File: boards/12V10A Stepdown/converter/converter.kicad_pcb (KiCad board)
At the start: 2 copper layers, 27 parts, among them J1 TB005-762-02BE, J2 TB005-762-02BE, M1 CSD17578Q3A, M2 CSD17571Q2, U1 LM25145RGYR

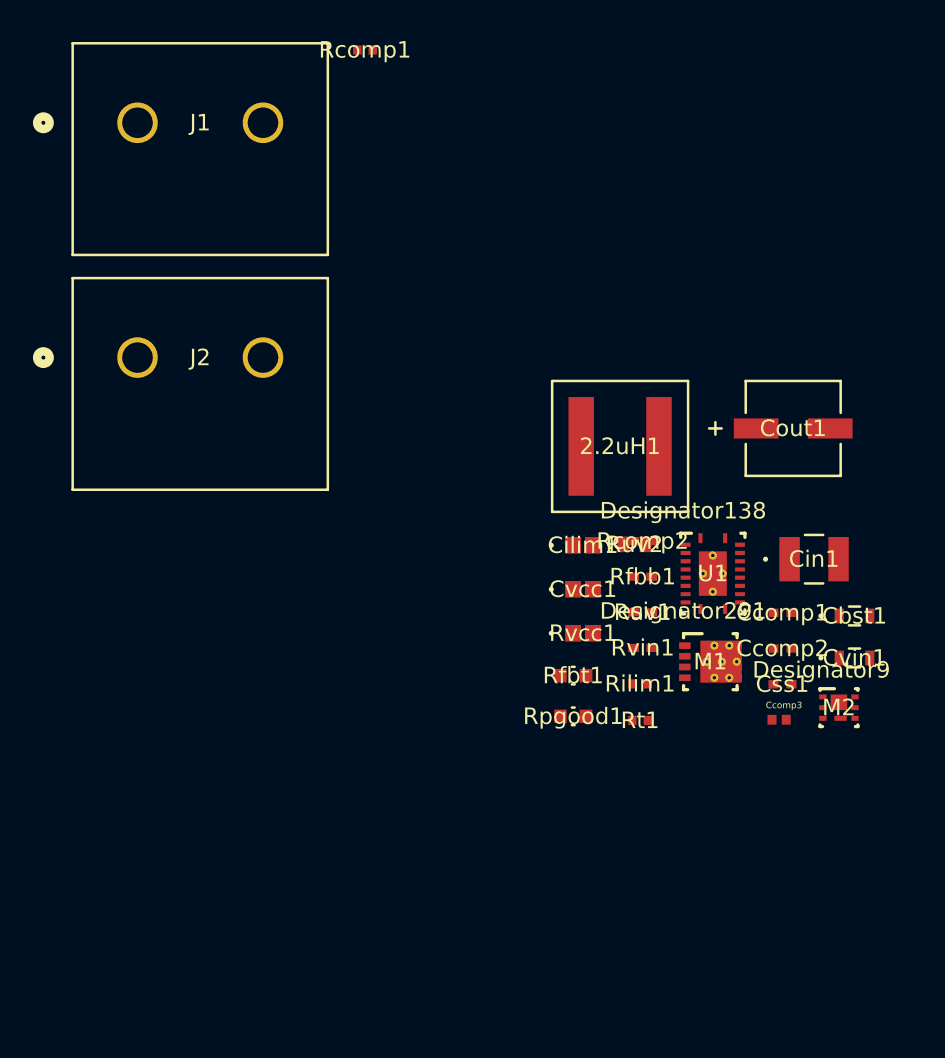
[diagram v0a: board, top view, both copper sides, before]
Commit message: 20A PCB partially traced
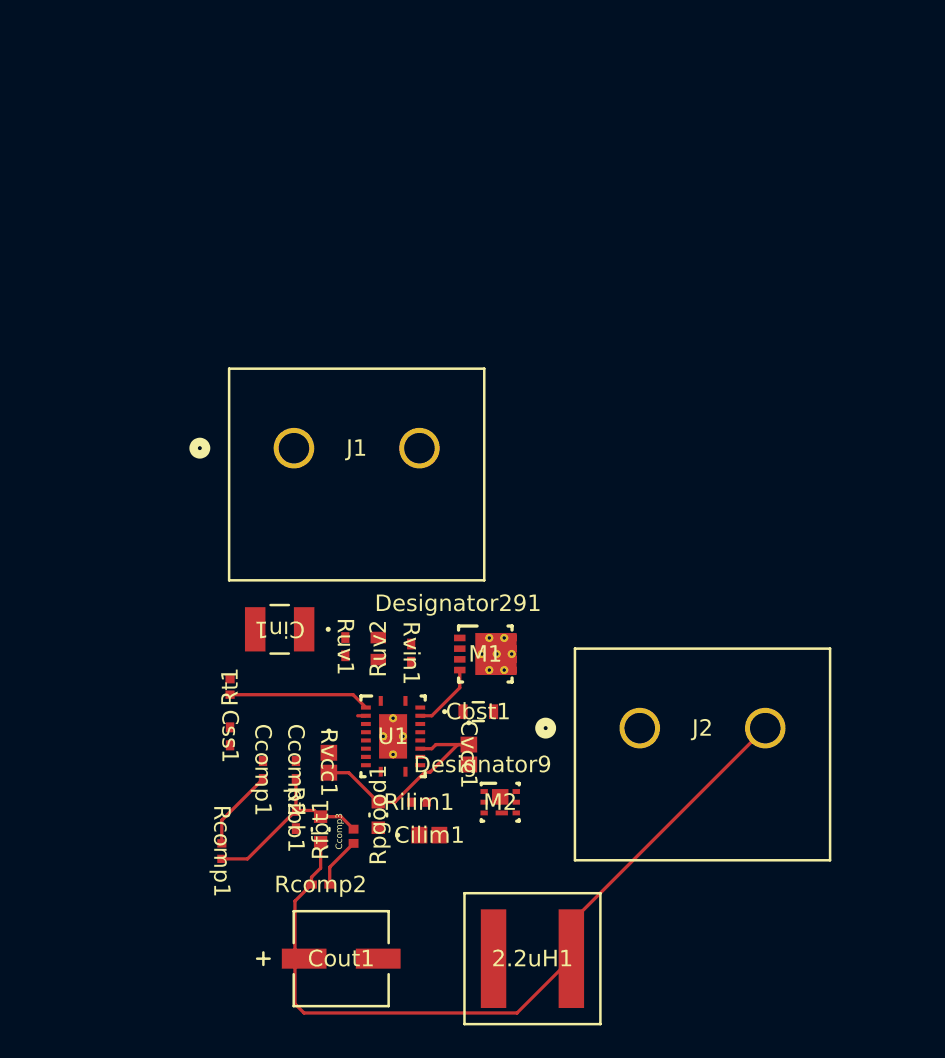
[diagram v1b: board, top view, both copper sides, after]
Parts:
- removed Cvin1: 100nF, 10A_LIbrary:CAP_1608_TDK
- moved Rcomp1 49.4 mm to (36.0, 70.0), turned to -90 degrees
- moved Cout1 42.3 mm to (43.2, 76.5)
- moved J2 37.9 mm to (61.4, 62.5)
- moved Css1 33.7 mm to (36.5, 63.0), turned to -90 degrees
- moved Ccomp1 33.0 mm to (38.5, 65.0), turned to -90 degrees
- moved Cin1 32.7 mm to (39.5, 56.5), turned to 180 degrees
- moved 2.2uH1 31.6 mm to (54.9, 76.5)
- moved Ccomp2 30.5 mm to (40.5, 65.0), turned to -90 degrees
- moved Rcomp2 28.6 mm to (42.0, 72.0)
- moved Ccomp3 26.8 mm to (44.0, 69.1), turned to 90 degrees
- moved Rfbb1 25.7 mm to (40.5, 68.1), turned to -90 degrees
- moved Rt1 25.0 mm to (36.5, 60.0), turned to 90 degrees
- moved Cbst1 23.6 mm to (51.6, 61.5)
- moved J1 21.9 mm to (40.4, 45.5)
- moved U1 21.8 mm to (46.4, 63.0)
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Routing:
- net Net-(2.2uH1-Pad2): track 0.00 -> 48.2 mm
- net Net-(U1-VCC): track 0.00 -> 13.7 mm
- net Net-(U1-FB): track 0.00 -> 11.6 mm
- net Net-(U1-RT): track 0.00 -> 8.57 mm
- net Net-(Ccomp1-Pad2): track 0.00 -> 4.94 mm
- net Net-(M1-G): track 0.00 -> 4.18 mm
- net Net-(Ccomp3-Pad1): track 0.00 -> 3.10 mm
- net Net-(U1-SS/TRK): track 0.00 -> 0.50 mm
